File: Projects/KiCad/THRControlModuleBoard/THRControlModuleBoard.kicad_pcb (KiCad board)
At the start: 2 copper layers, 9 parts, among them Q1 Q_PMOS_GDS, Q2 Q_PMOS_GDS, Q3 Q_PMOS_GDS, U1 LTC4416EMS#PBF

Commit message: THRControlModuleBoard
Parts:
- added C3: 0.1uF, Capacitor_SMD:C_0805_2012Metric_Pad1.18x1.45mm_HandSolder, F.Cu at (181.9, 87.9)
- added C4: 0.1uF, Capacitor_SMD:C_0805_2012Metric_Pad1.18x1.45mm_HandSolder, F.Cu at (181.9, 91.7)
- added C5: 0.1uF, Capacitor_SMD:C_0805_2012Metric_Pad1.18x1.45mm_HandSolder, F.Cu at (183.4, 81.0)
- added C6: 0.01uF, Capacitor_SMD:C_0805_2012Metric_Pad1.18x1.45mm_HandSolder, F.Cu at (181.9, 84.1)
- added C7: 0.01uF, Capacitor_SMD:C_0805_2012Metric_Pad1.18x1.45mm_HandSolder, F.Cu at (186.7, 76.2)
- added D1: D, Diode_SMD:D_0805_2012Metric_Pad1.15x1.40mm_HandSolder, F.Cu at (197.9, 91.7)
- added D2: D, Diode_SMD:D_0805_2012Metric_Pad1.15x1.40mm_HandSolder, F.Cu at (194.8, 91.7)
- added D3: D, Diode_SMD:D_0805_2012Metric_Pad1.15x1.40mm_HandSolder, F.Cu at (200.9, 91.7)
- added R4: 100, Resistor_SMD:R_0805_2012Metric_Pad1.20x1.40mm_HandSolder, F.Cu at (191.5, 81.0)
- added R5: 100, Resistor_SMD:R_0805_2012Metric_Pad1.20x1.40mm_HandSolder, F.Cu at (187.5, 81.0)
- added R6: 10k, Resistor_SMD:R_0805_2012Metric_Pad1.20x1.40mm_HandSolder, F.Cu at (197.9, 84.8)
- added R7: 10k, Resistor_SMD:R_0805_2012Metric_Pad1.20x1.40mm_HandSolder, F.Cu at (194.8, 84.9)
- added R8: 10k, Resistor_SMD:R_0805_2012Metric_Pad1.20x1.40mm_HandSolder, F.Cu at (200.9, 84.9)
- added U2: MAX31856MUD+T, Package_SO:TSSOP-14_4.4x5mm_P0.65mm, F.Cu at (187.5, 87.4)
- moved C2 25.6 mm to (168.1, 95.0)
- moved C1 17.5 mm to (153.7, 79.0), turned to 180 degrees
- moved Q3 14.6 mm to (156.1, 97.7)
- moved Q2 4.49 mm to (173.3, 68.6), turned to 0 degrees
- moved Q1 2.17 mm to (165.6, 78.0), turned to 180 degrees
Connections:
- net Net-(Q1-S) renamed /QMOS/3-3
- U1 pad 4: GND -> unconnected-(U1-*E2-Pad4)
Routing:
- net /QMOS/3-3: track 37.9 -> 6.05 mm
- net Main Power Supply: track 21.7 -> 0.00 mm
- net Net-(Q3-G): track 27.0 -> 15.6 mm, vias 0 -> 2
- net External Power Supply: track 14.1 -> 23.2 mm
- net +3.3V: track 0.00 -> 5.85 mm
- net Net-(U2-T+): track 0.00 -> 3.68 mm
- net Internal Power Supply: track 14.6 -> 15.7 mm
- net Net-(Q1-G): track 34.2 -> 35.1 mm, vias 2 -> 3
- added copper zone on F.Cu, net /QMOS/3-3
- removed copper zone on F.Cu, net Internal Power Supply

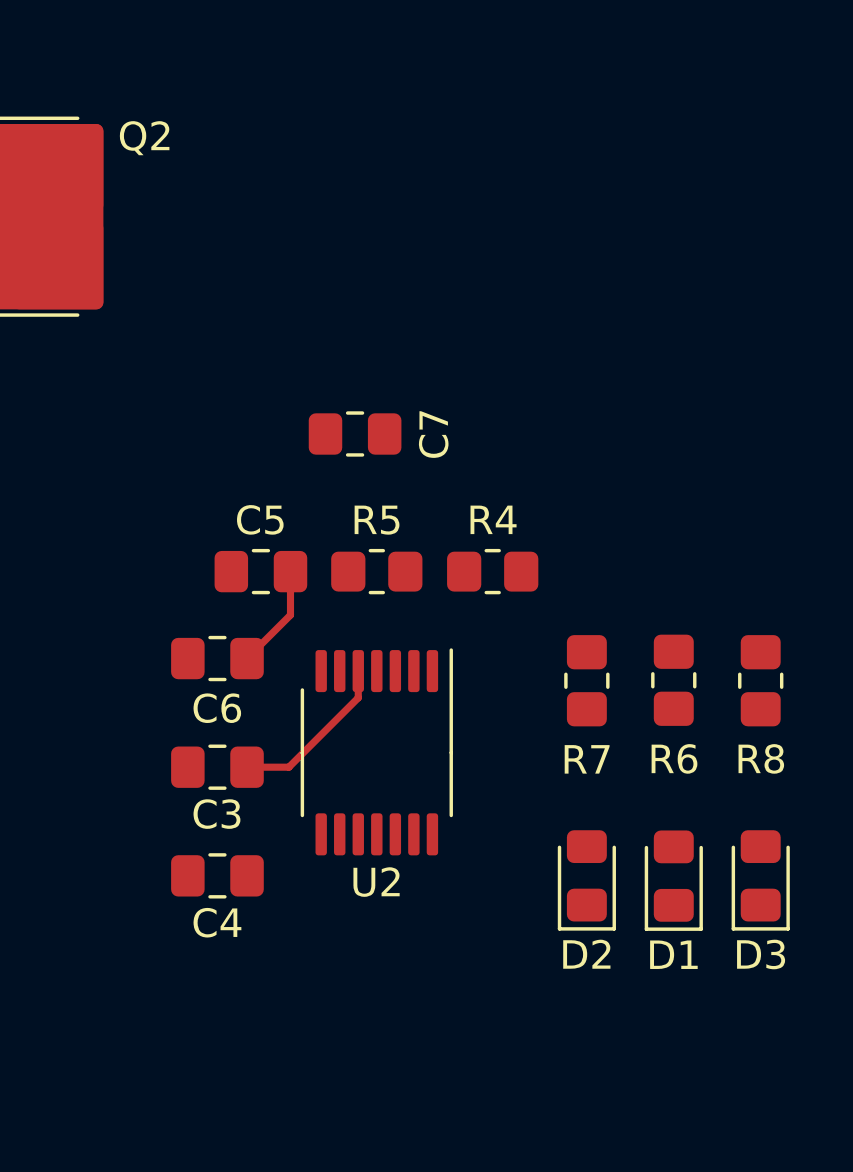
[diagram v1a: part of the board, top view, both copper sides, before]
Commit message: THRControlModuleBoardに熱電対アンプモジュールを追加しました。
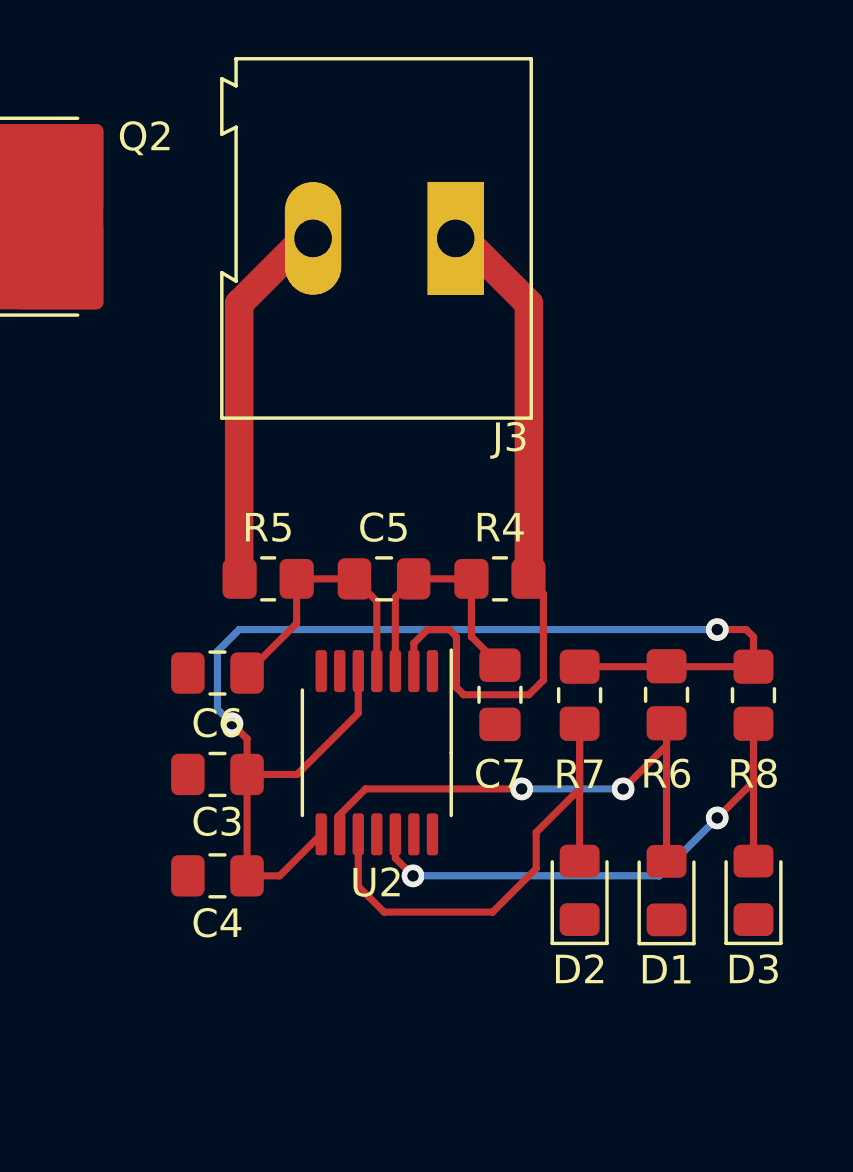
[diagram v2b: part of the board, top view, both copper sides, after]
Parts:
- added J3: Screw_Terminal_01x02, TerminalBlock:TerminalBlock_Altech_AK300-2_P5.00mm, F.Cu at (190.2, 69.3)
- moved C7 10.5 mm to (191.8, 85.3), turned to -90 degrees
- moved C5 4.33 mm to (187.7, 81.3), turned to 0 degrees
- moved R5 3.82 mm to (183.6, 81.3)
- moved D1 0.57 mm to (197.6, 92.2)
- moved D2 0.57 mm to (194.6, 92.2)
- moved R6 0.57 mm to (197.6, 85.3)
- moved R7 0.57 mm to (194.6, 85.4)
- moved D3 0.57 mm to (200.7, 92.2)
- moved R8 0.57 mm to (200.7, 85.4)
- moved C6 0.51 mm to (181.9, 84.6)
- moved R4 0.36 mm to (191.8, 81.3)
- moved C3 0.25 mm to (181.9, 88.1)
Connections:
- C5 pad 2: Net-(C5-Pad2) -> Net-(U2-T-)
- C7 pad 1: Net-(C5-Pad2) -> Net-(U2-T-)
- R5 pad 1: /THERM+ -> Net-(J3-Pin_2)
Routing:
- net +3.3V: track 5.85 -> 44.2 mm, vias 0 -> 2
- net BIAS: track 0.00 -> 24.9 mm
- net Net-(D3-A): track 0.00 -> 21.9 mm, vias 0 -> 2
- net Net-(D2-A): track 0.00 -> 19.6 mm
- net Net-(D1-A): track 0.00 -> 18.8 mm, vias 0 -> 2
- net Net-(J3-Pin_2): track 0.00 -> 13.2 mm
- net Net-(U2-T-): track 0.00 -> 9.09 mm
- net Net-(U2-T+): track 3.68 -> 9.61 mm

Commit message: THRControlModuleBoardの更新
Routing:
- net Net-(D1-A): track 18.8 -> 19.8 mm
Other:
- board outline added: 81.8 x 76.2 mm
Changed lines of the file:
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@@
-        (effects (font (size 1 1) (thickness 0.15)))
-    )
-    (fp_text user "${REFERENCE}" (at 0 0 90) (layer "F.Fab")
         (effects (font (size 1 1) (thickness 0.15)))
     )
@@
     )
   )
+  (gr_rect (start 127 51.054) (end 208.788 127.254)
+    (stroke (width 0.1) (type default)) (fill none) (layer "Edge.Cuts"))
   (segment (start 163.392 78.994) (end 164.408 77.978) (width 0.25) (layer "F.Cu") (net 1))
   (segment (start 160.782 83.312) (end 160.02 82.55) (width 0.25) (layer "F.Cu") (net 1))
@@
   (segment (start 188.7435 81.28) (end 188.102 81.9215) (width 0.25) (layer "F.Cu") (net 13))
   (segment (start 197.612 87.122) (end 197.612 86.344) (width 0.25) (layer "F.Cu") (net 14))
+  (segment (start 191.77 89.916) (end 190.5 88.646) (width 0.25) (layer "F.Cu") (net 14))
+  (segment (start 187.055959 88.646) (end 186.152 89.549959) (width 0.25) (layer "F.Cu") (net 14))
+  (segment (start 186.152 89.549959) (end 186.152 90.2385) (width 0.25) (layer "F.Cu") (net 14))
   (segment (start 196.088 88.646) (end 197.612 87.122) (width 0.25) (layer "F.Cu") (net 14))
-  (segment (start 186.152 90.2385) (end 186.152 89.549959) (width 0.25) (layer "F.Cu") (net 14))
-  (segment (start 186.152 89.549959) (end 187.055959 88.646) (width 0.25) (layer "F.Cu") (net 14))
+  (segment (start 190.5 88.646) (end 187.055959 88.646) (width 0.25) (layer "F.Cu") (net 14))
   (segment (start 197.612 86.344) (end 197.612 91.186) (width 0.25) (layer "F.Cu") (net 14))
-  (segment (start 187.055959 88.646) (end 192.532 88.646) (width 0.25) (layer "F.Cu") (net 14))
-  (via (at 192.532 88.646) (size 0.8) (drill 0.4) (layers "F.Cu" "B.Cu") (net 14))
+  (via (at 191.77 89.916) (size 0.8) (drill 0.4) (layers "F.Cu" "B.Cu") (net 14))
   (via (at 196.088 88.646) (size 0.8) (drill 0.4) (layers "F.Cu" "B.Cu") (net 14))
-  (segment (start 192.532 88.646) (end 196.088 88.646) (width 0.25) (layer "B.Cu") (net 14))
+  (segment (start 193.04 88.646) (end 196.088 88.646) (width 0.25) (layer "B.Cu") (net 14))
+  (segment (start 191.77 89.916) (end 193.04 88.646) (width 0.25) (layer "B.Cu") (net 14))
   (segment (start 193.04 90.17) (end 194.564 88.646) (width 0.25) (layer "F.Cu") (net 15))
   (segment (start 194.564 86.36) (end 194.564 91.177) (width 0.25) (layer "F.Cu") (net 15))

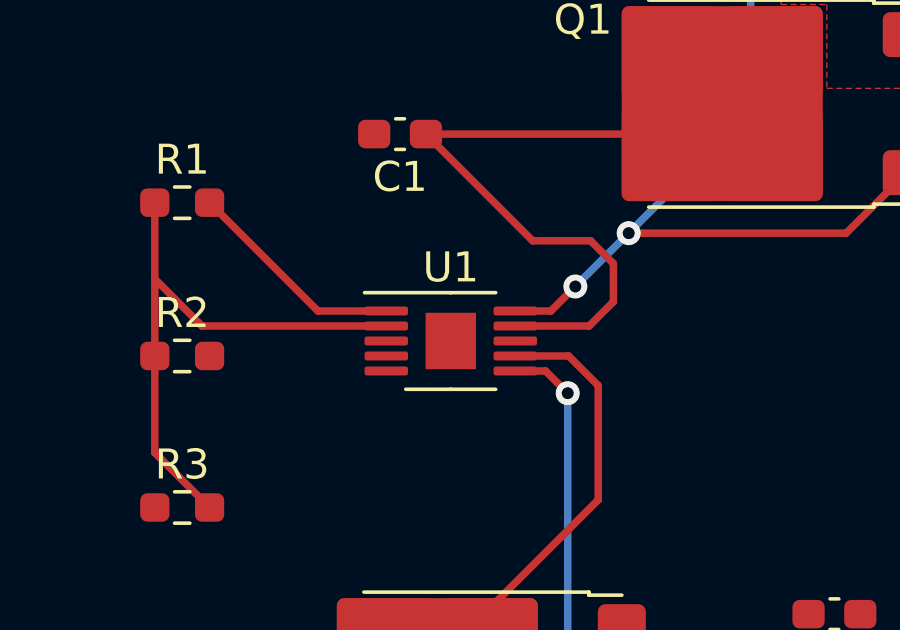
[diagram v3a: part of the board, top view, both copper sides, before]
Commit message: STM32F303K8のシートを追加
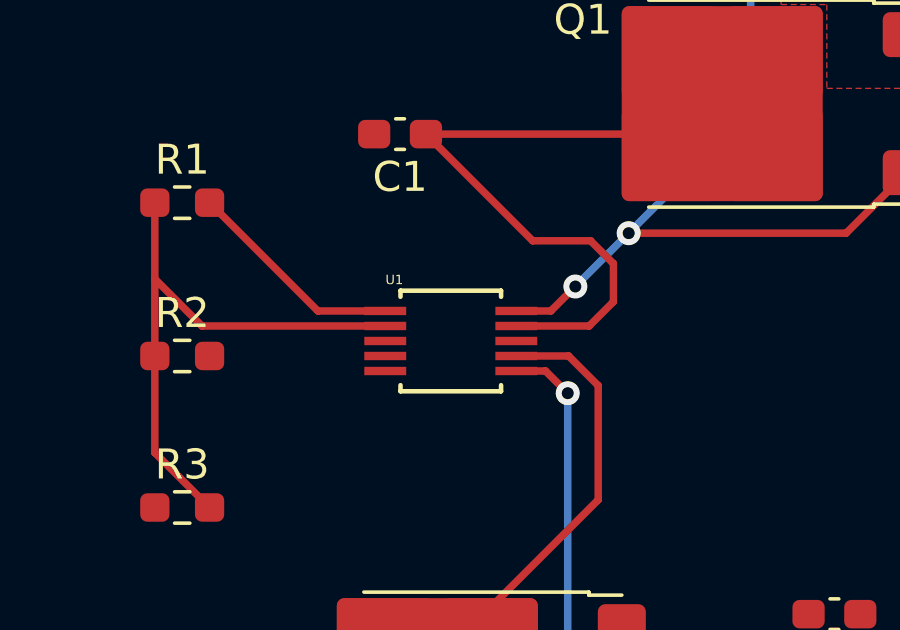
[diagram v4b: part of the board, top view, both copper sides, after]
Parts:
- U1: footprint Package_SO:MSOP-10-1EP_3x3mm_P0.5mm_EP1.68x1.88mm -> LTC4416EMS#PBF:MSOP-10_MS
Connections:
- net CS renamed /STM32F303K8/SPI__~{CS}-~{CS}
- net SCK renamed /STM32F303K8/SPI__SCK-SCLK
- net SDI renamed /STM32F303K8/SPI__SDI-MOSI
- net SDO renamed /STM32F303K8/SPI__SDO-MISO

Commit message: THRControlModuleBoardを更新
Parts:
- added J1: Conn_01x02_Socket, CONNECTOR:CONNECTOR_2, F.Cu at (126.2, 108.4)
- added J2: Conn_01x02_Socket, CONNECTOR:CONNECTOR_2, F.Cu at (134.4, 108.4)
- added U3: NUCLEO-F303K8, NUCLEO-F303K8:MODULE_NUCLEO-F303K8, F.Cu at (173.9, 114.0)
- U1: footprint LTC4416EMS#PBF:MSOP-10_MS -> Package_SO:MSOP-10_3x3mm_P0.5mm
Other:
- board size 81.8 x 76.2 mm -> 119.8 x 119.8 mm

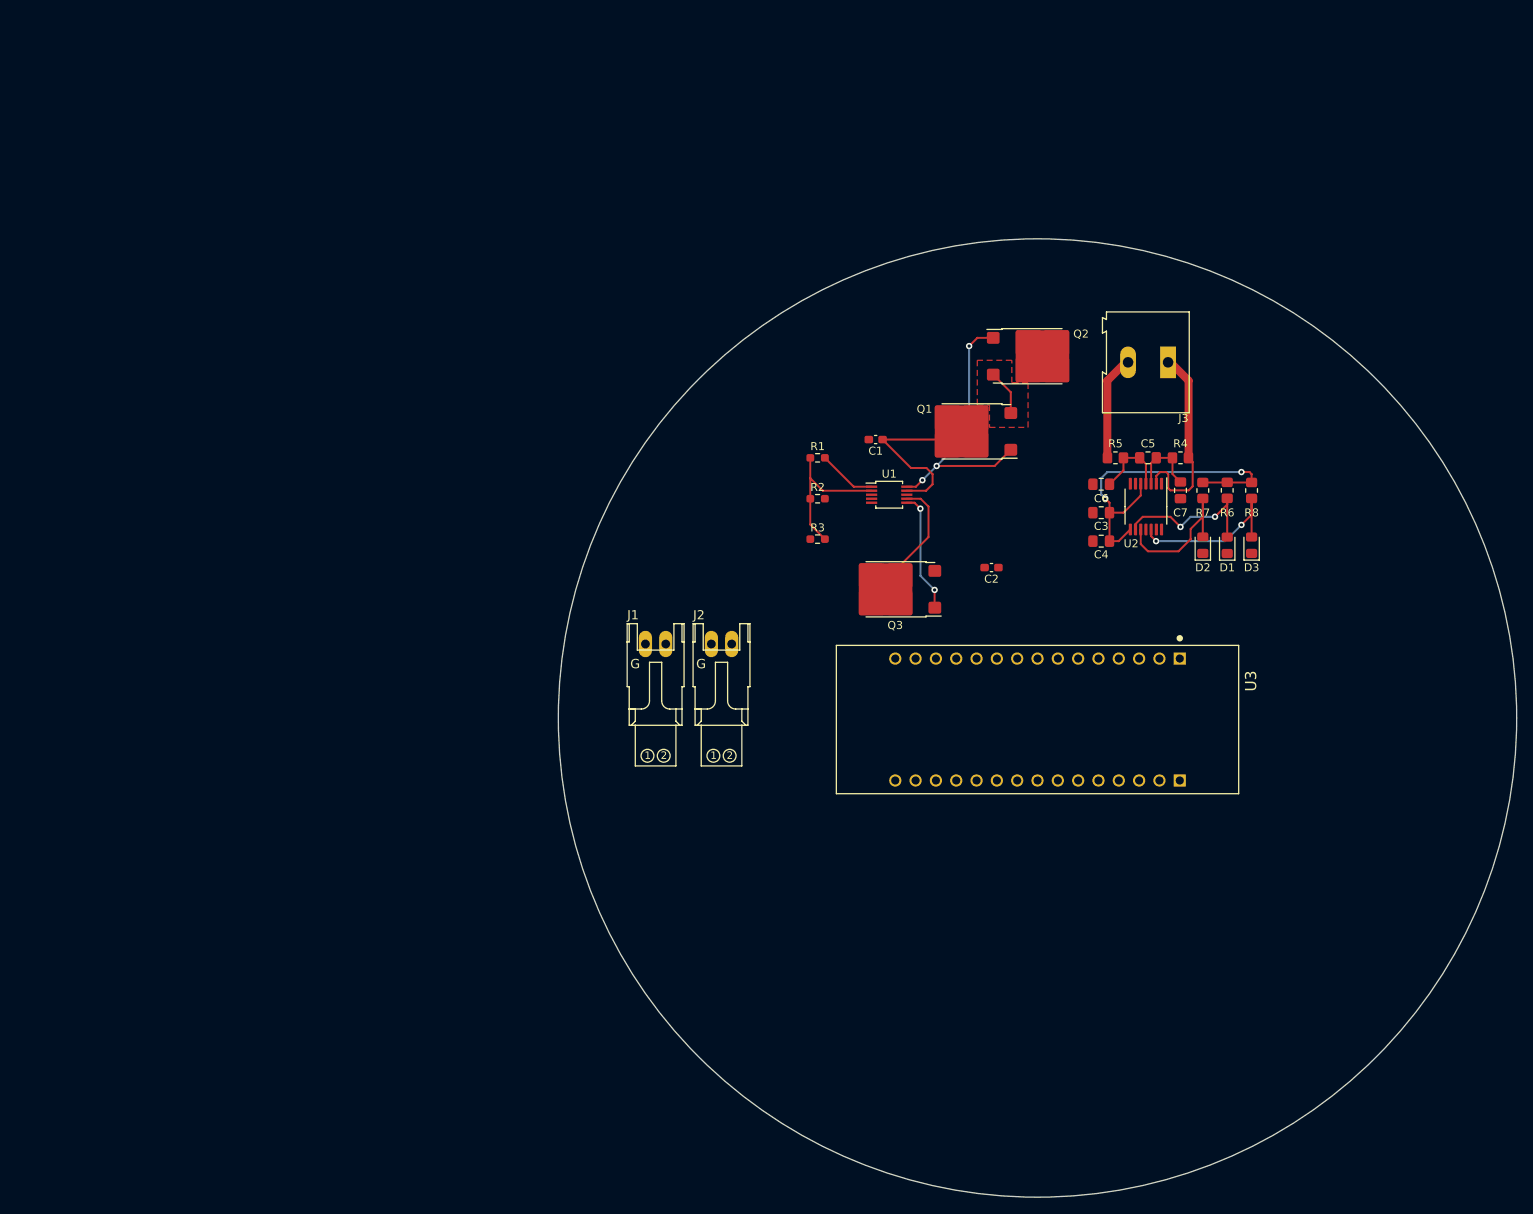
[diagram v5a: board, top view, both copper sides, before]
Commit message: THRControlModuleBoardにRS485系統を追加しました。
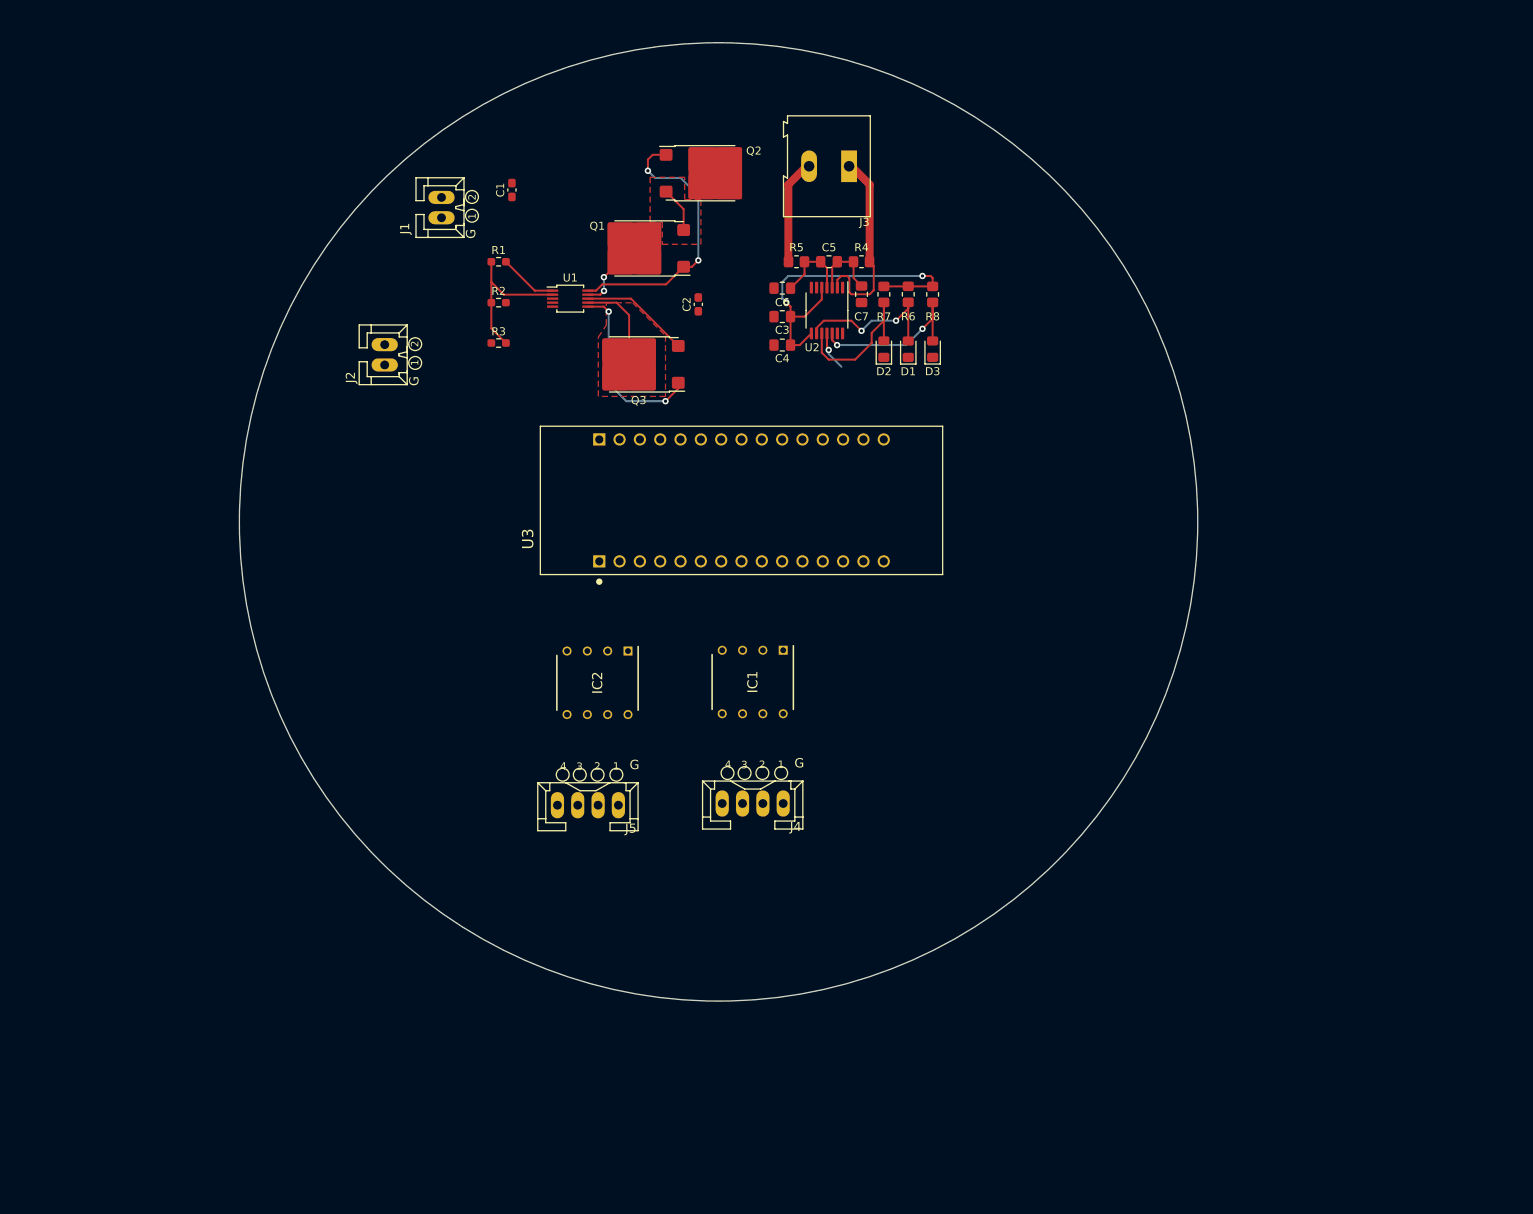
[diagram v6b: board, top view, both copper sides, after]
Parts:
- added IC1: LTC1480CN8#PBF, LTC1480CN8#PBF:DIP794W53P254L1016H394Q8N, F.Cu at (138.3, 109.3)
- added IC2: LTC1480CN8#PBF, LTC1480CN8#PBF:DIP794W53P254L1016H394Q8N, F.Cu at (118.9, 109.4)
- added J4: Conn_01x04_Socket, CONNECTOR:CONNECTOR_4-STRAIGHT, F.Cu at (138.3, 124.5)
- added J5: Conn_01x04_Socket, CONNECTOR:CONNECTOR_4-STRAIGHT, F.Cu at (117.7, 124.7)
- J1, J2: footprint CONNECTOR:CONNECTOR_2 -> CONNECTOR:CONNECTOR_2-STRAIGHT
- moved J1 64.2 mm to (99.4, 50.0), turned to 90 degrees
- moved J2 58.0 mm to (92.3, 68.4), turned to 90 degrees
- moved C1 55.1 mm to (108.2, 47.8), turned to 90 degrees
- moved C2 49.2 mm to (131.5, 62.1), turned to 90 degrees
- moved Q1 46.9 mm to (124.7, 55.1)
- moved Q2 46.9 mm to (132.4, 45.7)
- moved U1 46.8 mm to (115.5, 61.4)
- moved C3 46.8 mm to (142.0, 63.6)
- moved C4 46.8 mm to (142.0, 67.2)
- moved C5 46.8 mm to (147.8, 56.8)
- moved D1 46.8 mm to (157.7, 67.7)
- moved D2 46.8 mm to (154.7, 67.7)
- moved D3 46.8 mm to (160.8, 67.7)
- moved J3 46.8 mm to (150.3, 44.8)
- moved R1 46.8 mm to (106.5, 56.8)
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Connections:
- net FAULT renamed ~{FAULT}
- U3 pad 3_1: unconnected-(U3A-PA9-Pad3_1) -> RS485__DI-TX
- U3 pad 3_2: unconnected-(U3A-PA10-Pad3_2) -> RS485__RO-RX
- U3 pad 3_5: unconnected-(U3A-PA12-Pad3_5) -> RS485__ENABLE
- U3 pad 3_9: unconnected-(U3A-PB1-Pad3_9) -> DRDY
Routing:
- net External Power Supply: track 23.2 -> 8.22 mm, vias 0 -> 2
- net Main Power Supply: track 0.00 -> 13.8 mm
- net Net-(Q3-G): track 15.6 -> 22.9 mm
- net /STM32F303K8/SPI__SDO-MISO: track 0.00 -> 4.92 mm, vias 0 -> 1
- net Internal Power Supply: track 15.7 -> 12.0 mm
- net Net-(D2-A): track 19.6 -> 20.4 mm
- net Net-(Q1-G): track 35.1 -> 35.0 mm, vias 3 -> 2
- added copper zone on F.Cu, net Internal Power Supply
